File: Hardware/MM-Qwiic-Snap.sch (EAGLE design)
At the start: 49 parts, among them J15 MICROMOD-2222-C, J2 QWIIC_RIGHT_ANGLE, U1 MCP73831, U2 4-40_SMD_STANDOFFSMD, U3 4-40_SMD_STANDOFFSMD, U4 4-40_SMD_STANDOFFSMD, U5 AP7361C-33FGEUDFN-8, U6 4-40_SMD_STANDOFFSMD

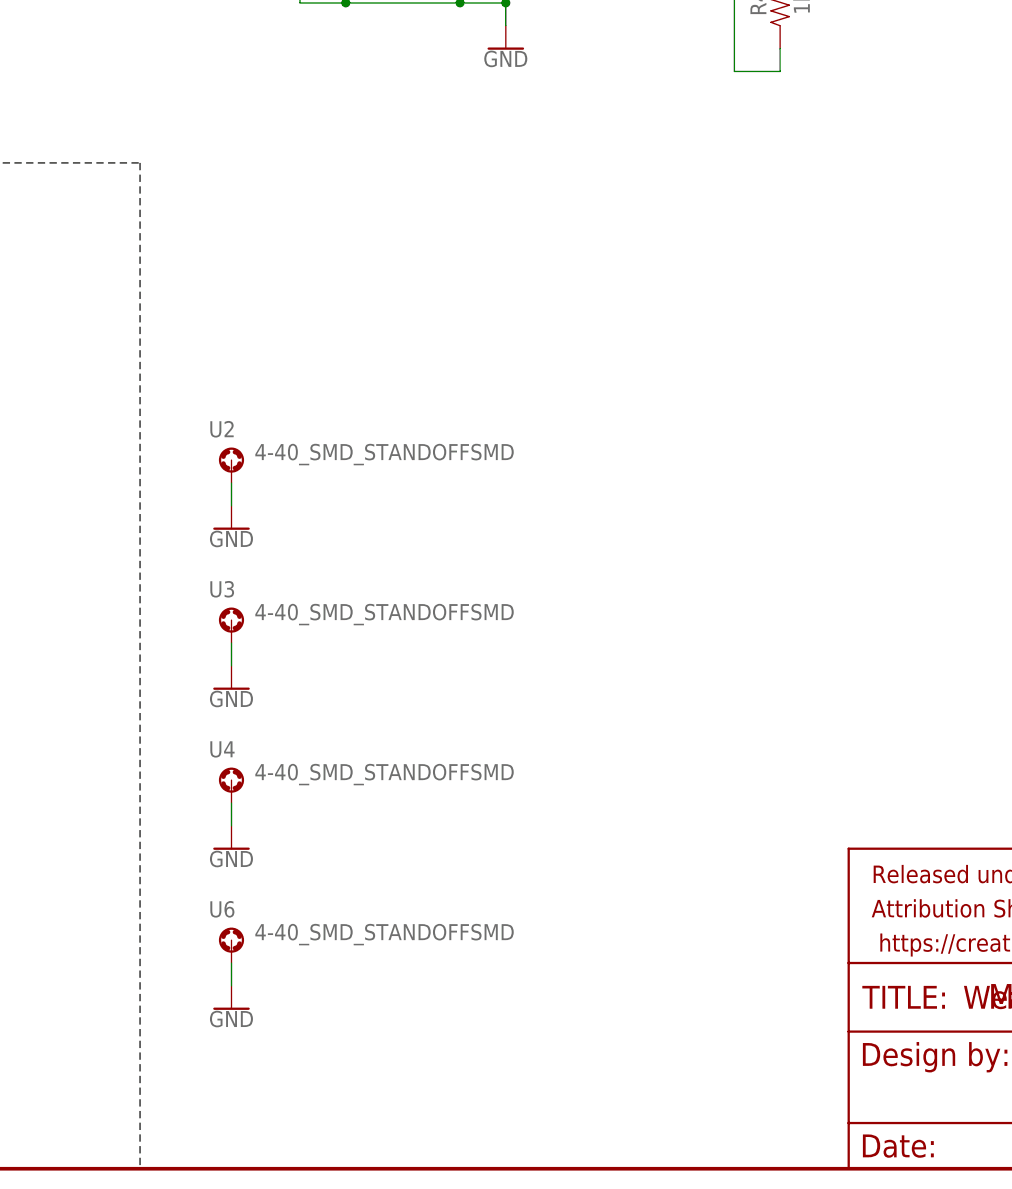
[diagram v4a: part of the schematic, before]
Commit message: Switch out stand offs
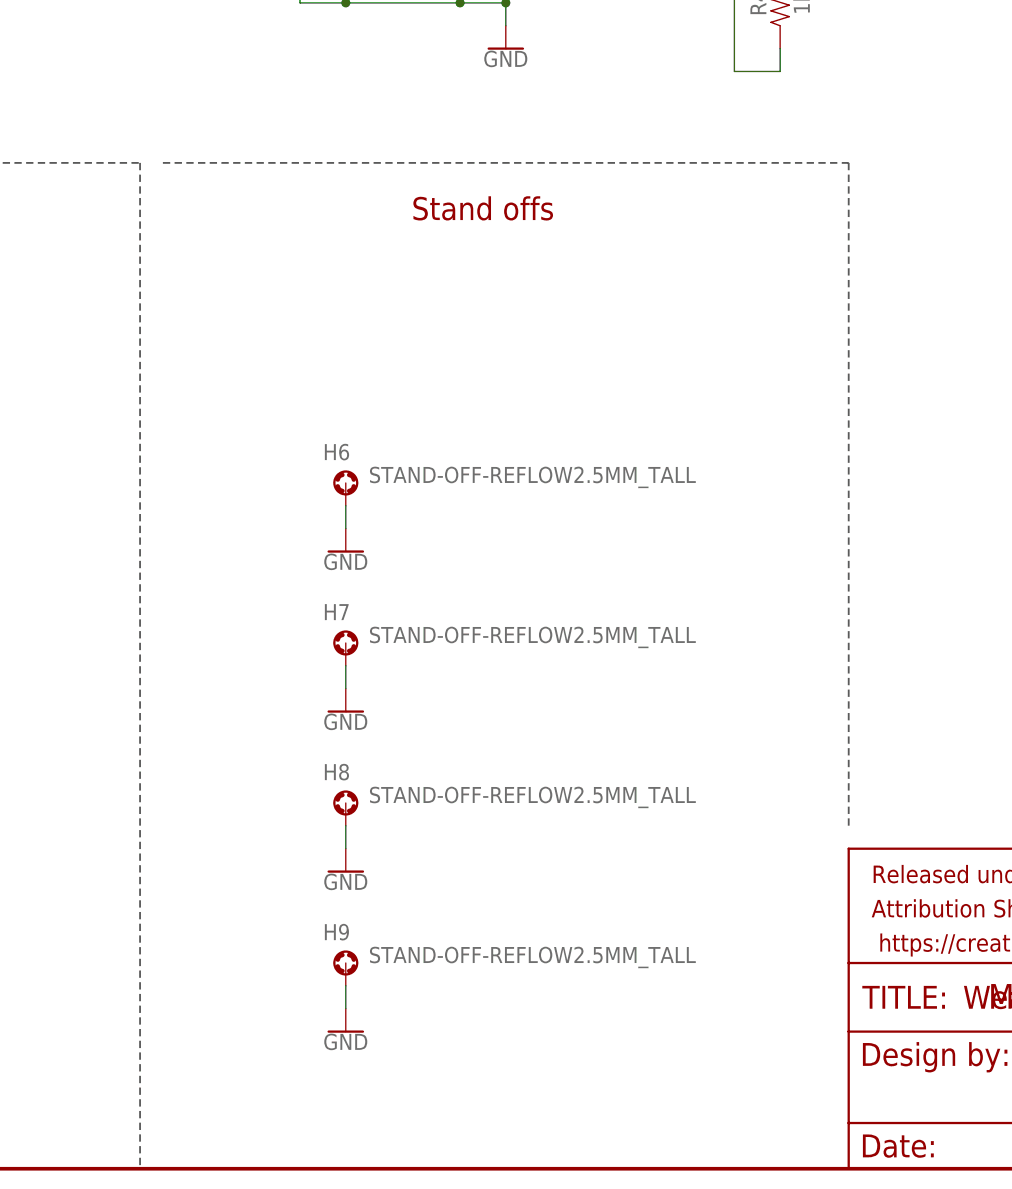
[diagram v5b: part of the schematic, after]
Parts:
- removed U2, U3, U4, U6: 4-40_SMD_STANDOFFSMD, qwiic_carrier:4-40_SMD_STANDOFFSMD
- added H6, H7, H8, H9: STAND-OFF-REFLOW2.5MM_TALL, SparkFun-Hardware:STAND-OFF-REFLOW2.5MM_TALL
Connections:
- net GND: now also H6.1, H7.1, H8.1, H9.1; no longer U2.1, U3.1, U4.1, U6.1
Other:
- note added: "Stand offs"
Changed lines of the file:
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@@
 <part name="SUPPLY8" library="SparkFun-PowerSymbols" deviceset="VIN" device=""/>
 <part name="SUPPLY9" library="SparkFun-PowerSymbols" deviceset="VIN" device=""/>
-<part name="U2" library="qwiic_carrier" deviceset="4-40_SMD_STANDOFF" device="SMD"/>
-<part name="U3" library="qwiic_carrier" deviceset="4-40_SMD_STANDOFF" device="SMD"/>
-<part name="U4" library="qwiic_carrier" deviceset="4-40_SMD_STANDOFF" device="SMD"/>
-<part name="U6" library="qwiic_carrier" deviceset="4-40_SMD_STANDOFF" device="SMD"/>
+<part name="H6" library="SparkFun-Hardware" deviceset="STAND-OFF-REFLOW" device="2.5MM_TALL"/>
+<part name="H7" library="SparkFun-Hardware" deviceset="STAND-OFF-REFLOW" device="2.5MM_TALL"/>
+<part name="H8" library="SparkFun-Hardware" deviceset="STAND-OFF-REFLOW" device="2.5MM_TALL"/>
+<part name="H9" library="SparkFun-Hardware" deviceset="STAND-OFF-REFLOW" device="2.5MM_TALL"/>
 <part name="GND7" library="SparkFun-PowerSymbols" deviceset="GND" device=""/>
 <part name="GND11" library="SparkFun-PowerSymbols" deviceset="GND" device=""/>
@@
 <text x="210.82" y="104.14" size="2.54" layer="94" align="center">Buttons</text>
 <text x="304.8" y="182.88" size="2.54" layer="94" align="center">Battery Charger</text>
+<text x="289.56" y="106.68" size="2.54" layer="94" align="center">Stand offs</text>
+<wire x1="254" y1="111.76" x2="330.2" y2="111.76" width="0.2032" layer="97" style="longdash"/>
+<wire x1="330.2" y1="111.76" x2="330.2" y2="38.1" width="0.2032" layer="97" style="longdash"/>
 </plain>
 <instances>
@@
 <attribute name="VALUE" x="22.86" y="239.014" size="1.778" layer="96" align="bottom-center"/>
 </instance>
-<instance part="U2" gate="U1" x="261.62" y="78.74" smashed="yes">
-<attribute name="NAME" x="259.08" y="81.28" size="1.778" layer="95"/>
-<attribute name="VALUE" x="264.16" y="78.74" size="1.778" layer="96"/>
-</instance>
-<instance part="U3" gate="U1" x="261.62" y="60.96" smashed="yes">
-<attribute name="NAME" x="259.08" y="63.5" size="1.778" layer="95"/>
-<attribute name="VALUE" x="264.16" y="60.96" size="1.778" layer="96"/>
-</instance>
-<instance part="U4" gate="U1" x="261.62" y="43.18" smashed="yes">
-<attribute name="NAME" x="259.08" y="45.72" size="1.778" layer="95"/>
-<attribute name="VALUE" x="264.16" y="43.18" size="1.778" layer="96"/>
-</instance>
-<instance part="U6" gate="U1" x="261.62" y="25.4" smashed="yes">
-<attribute name="NAME" x="259.08" y="27.94" size="1.778" layer="95"/>
-<attribute name="VALUE" x="264.16" y="25.4" size="1.778" layer="96"/>
-</instance>
-<instance part="GND7" gate="1" x="261.62" y="71.12" smashed="yes">
-<attribute name="VALUE" x="261.62" y="70.866" size="1.778" layer="96" align="top-center"/>
-</instance>
-<instance part="GND11" gate="1" x="261.62" y="53.34" smashed="yes">
-<attribute name="VALUE" x="261.62" y="53.086" size="1.778" layer="96" align="top-center"/>
-</instance>
-<instance part="GND12" gate="1" x="261.62" y="35.56" smashed="yes">
-<attribute name="VALUE" x="261.62" y="35.306" size="1.778" layer="96" align="top-center"/>
-</instance>
-<instance part="GND13" gate="1" x="261.62" y="17.78" smashed="yes">
-<attribute name="VALUE" x="261.62" y="17.526" size="1.778" layer="96" align="top-center"/>
+<instance part="H6" gate="G$1" x="274.32" y="76.2" smashed="yes">
+<attribute name="NAME" x="271.78" y="78.74" size="1.778" layer="95"/>
+<attribute name="VALUE" x="276.86" y="76.2" size="1.778" layer="96"/>
+</instance>
+<instance part="H7" gate="G$1" x="274.32" y="58.42" smashed="yes">
+<attribute name="NAME" x="271.78" y="60.96" size="1.778" layer="95"/>
+<attribute name="VALUE" x="276.86" y="58.42" size="1.778" layer="96"/>
+</instance>
+<instance part="H8" gate="G$1" x="274.32" y="40.64" smashed="yes">
+<attribute name="NAME" x="271.78" y="43.18" size="1.778" layer="95"/>
+<attribute name="VALUE" x="276.86" y="40.64" size="1.778" layer="96"/>
+</instance>
+<instance part="H9" gate="G$1" x="274.32" y="22.86" smashed="yes">
+<attribute name="NAME" x="271.78" y="25.4" size="1.778" layer="95"/>
+<attribute name="VALUE" x="276.86" y="22.86" size="1.778" layer="96"/>
+</instance>
+<instance part="GND7" gate="1" x="274.32" y="68.58" smashed="yes">
+<attribute name="VALUE" x="274.32" y="68.326" size="1.778" layer="96" align="top-center"/>
+</instance>
+<instance part="GND11" gate="1" x="274.32" y="50.8" smashed="yes">
+<attribute name="VALUE" x="274.32" y="50.546" size="1.778" layer="96" align="top-center"/>
+</instance>
+<instance part="GND12" gate="1" x="274.32" y="33.02" smashed="yes">
+<attribute name="VALUE" x="274.32" y="32.766" size="1.778" layer="96" align="top-center"/>
+</instance>
+<instance part="GND13" gate="1" x="274.32" y="15.24" smashed="yes">
+<attribute name="VALUE" x="274.32" y="14.986" size="1.778" layer="96" align="top-center"/>
 </instance>
 </instances>
@@
 </segment>
 <segment>
-<pinref part="U2" gate="U1" pin="1"/>
+<pinref part="H6" gate="G$1" pin="1"/>
 <pinref part="GND7" gate="1" pin="GND"/>
-<wire x1="261.62" y1="73.66" x2="261.62" y2="76.2" width="0.1524" layer="91"/>
-</segment>
-<segment>
-<pinref part="U3" gate="U1" pin="1"/>
+<wire x1="274.32" y1="71.12" x2="274.32" y2="73.66" width="0.1524" layer="91"/>
+</segment>
+<segment>
+<pinref part="H7" gate="G$1" pin="1"/>
 <pinref part="GND11" gate="1" pin="GND"/>
-<wire x1="261.62" y1="55.88" x2="261.62" y2="58.42" width="0.1524" layer="91"/>
-</segment>
-<segment>
-<pinref part="U4" gate="U1" pin="1"/>
+<wire x1="274.32" y1="53.34" x2="274.32" y2="55.88" width="0.1524" layer="91"/>
+</segment>
+<segment>
+<pinref part="H8" gate="G$1" pin="1"/>
 <pinref part="GND12" gate="1" pin="GND"/>
-<wire x1="261.62" y1="38.1" x2="261.62" y2="40.64" width="0.1524" layer="91"/>
-</segment>
-<segment>
-<pinref part="U6" gate="U1" pin="1"/>
+<wire x1="274.32" y1="35.56" x2="274.32" y2="38.1" width="0.1524" layer="91"/>
+</segment>
+<segment>
+<pinref part="H9" gate="G$1" pin="1"/>
 <pinref part="GND13" gate="1" pin="GND"/>
-<wire x1="261.62" y1="20.32" x2="261.62" y2="22.86" width="0.1524" layer="91"/>
+<wire x1="274.32" y1="17.78" x2="274.32" y2="20.32" width="0.1524" layer="91"/>
 </segment>
 </net>
